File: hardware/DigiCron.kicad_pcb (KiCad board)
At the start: 2 copper layers, 36 x 36 mm, 6 parts, among them U100 MDBT50Q-U1MV2, U101 HCMS-3917, U102 HCMS-3917, X100 12401598E4#2A

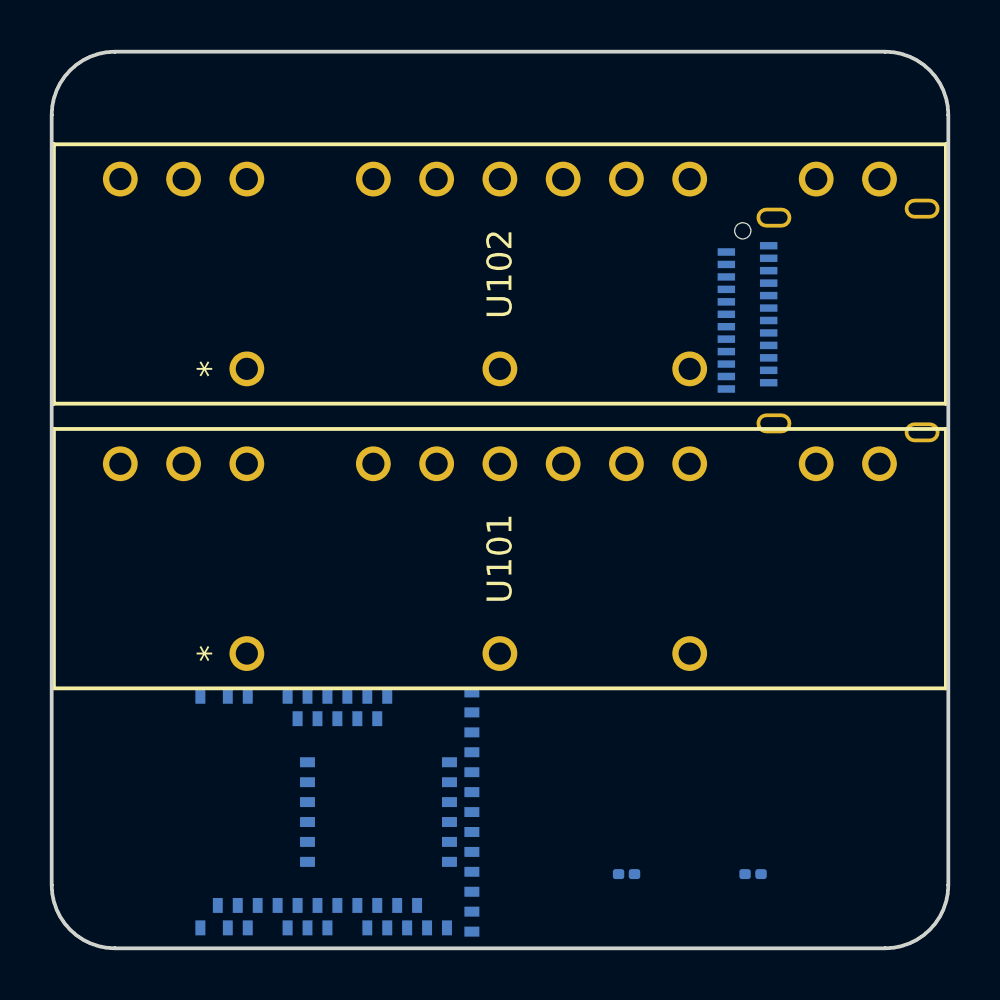
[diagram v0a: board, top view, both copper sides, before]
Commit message: Add some sensor ICs to schematic
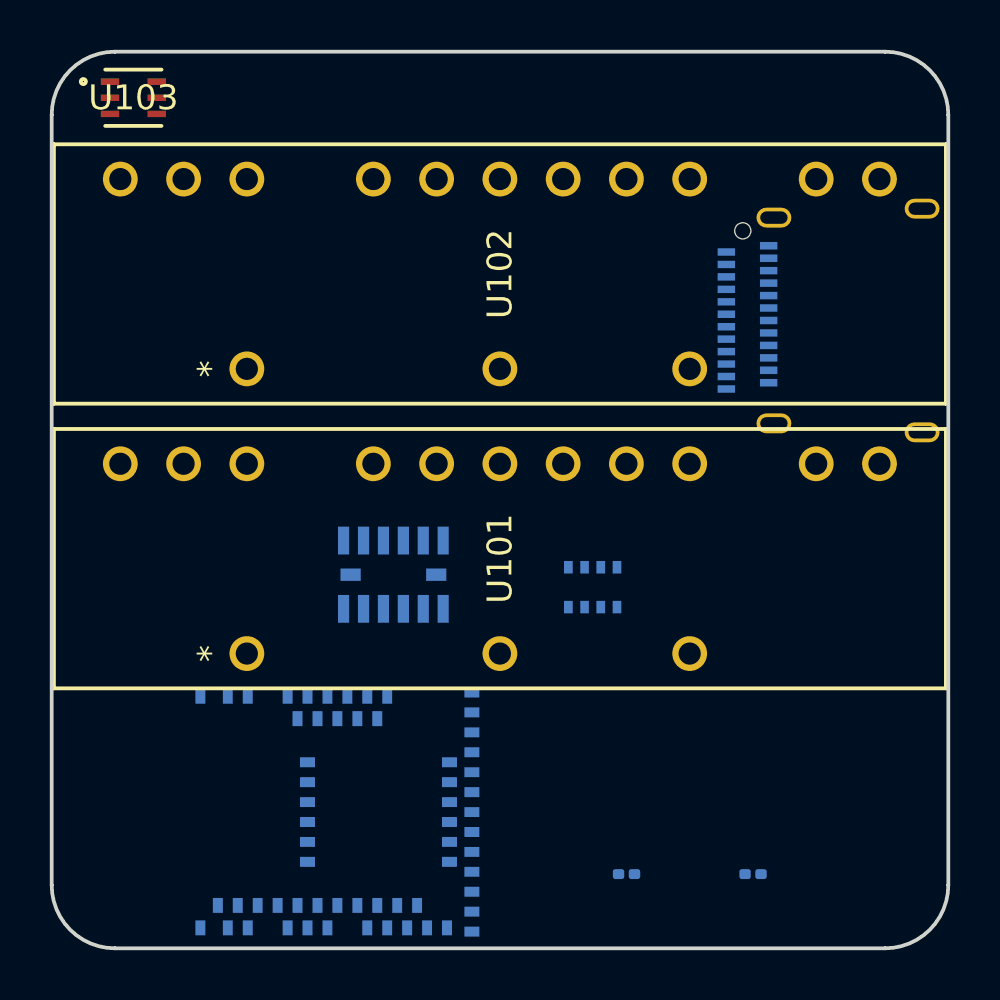
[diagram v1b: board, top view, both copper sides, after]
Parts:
- added U103: LTR-390UV-01, LTR390:SMD6_LTR-390UV-01_LTO, F.Cu at (183.2, 67.9)
- added U104: ADXL345BCCZ-RL, ADXL345:LGA_CC-14-1_ADI, B.Cu at (193.6, 87.0)
- added U105: BMP280, Package_LGA:Bosch_LGA-8_2x2.5mm_P0.65mm_ClockwisePinNumbering, B.Cu at (201.6, 87.5)
- U101, U102: footprint footprints:DIP26_HCMS-290X-B_BRA -> HCMS-x91x:DIP26_HCMS-290X-B_BRA

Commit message: Replace BMP280 with BME280 and add IR LED and JST connector
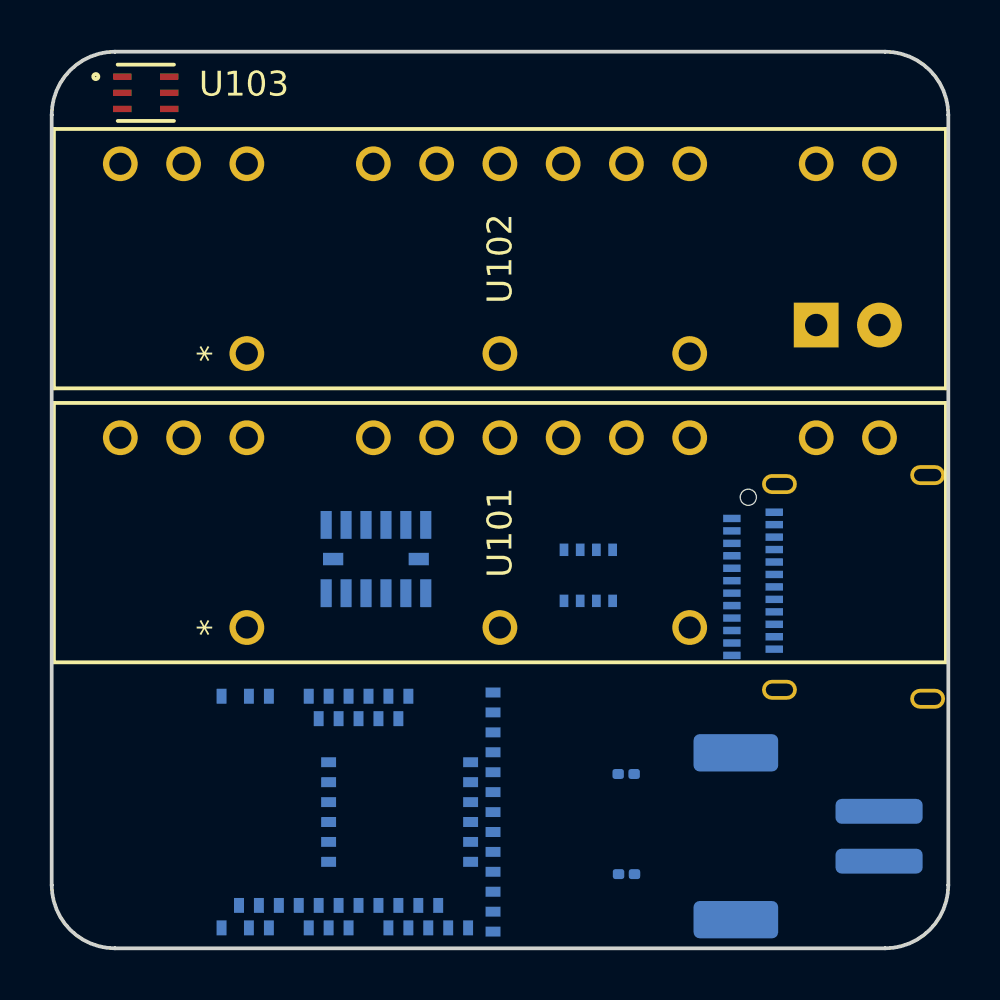
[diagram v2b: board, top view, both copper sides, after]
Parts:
- added D100: IR LED, LED_THT:LED_D5.0mm_Horizontal_O1.27mm_Z3.0mm_IRBlack, B.Cu at (210.6, 77.0)
- added J100: Conn_Receptacle_2P, Connector_JST:JST_PH_S2B-PH-SM4-TB_1x02-1MP_P2.00mm_Horizontal, B.Cu at (210.3, 97.5)
- U105: value BMP280 -> BME280; footprint Package_LGA:Bosch_LGA-8_2x2.5mm_P0.65mm_ClockwisePinNumbering -> Package_LGA:Bosch_LGA-8_2.5x2.5mm_P0.65mm_ClockwisePinNumbering
- moved X100 10.7 mm to (207.9, 87.5)
- moved R100 6.49 mm to (203.0, 95.0)
- moved U101 1.05 mm to (187.7, 89.2)
- moved U104 0.94 mm to (192.9, 86.4)
- moved U100 0.85 mm to (190.5, 96.6)
- moved U102 0.62 mm to (187.7, 78.2)
- moved U103 0.54 mm to (183.7, 67.7)
- moved U105 0.51 mm to (201.4, 87.1)
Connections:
- net /D12 renamed /IR_IN
- net /D13 renamed /JOY_SELECT
- net /D5 renamed /JOY_HOME
- net /D6 renamed /JOY_BACK
- U100 pad 16: /D10 -> unconnected-(U100-P0.27-Pad16)
- U100 pad 19: /D9 -> unconnected-(U100-P0.26-Pad19)
- U100 pad 22: /D11 -> /IR_OUT
- U100 pad 5: unconnected-(U100-P1.12-Pad5) -> /JOY_UP
- U100 pad 6: unconnected-(U100-P1.13-Pad6) -> /JOY_LEFT
- U100 pad 7: unconnected-(U100-P1.14-Pad7) -> /JOY_RIGHT
- U100 pad 8: unconnected-(U100-P1.15-Pad8) -> /JOY_DOWN
